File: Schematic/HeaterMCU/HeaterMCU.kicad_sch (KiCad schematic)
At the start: 59 parts, among them J301 To PSU Board, J302 Heater Control, J303 High voltage warning, J304 Firmware, SW301 RESET, U301 Display_IPS_1.3_SPI, U302 ATMEGA328P-AU, U303 TLP185, U304 INA219AIDCNR, U305 TLP185, U306 TPS54302, Y301 8MHz

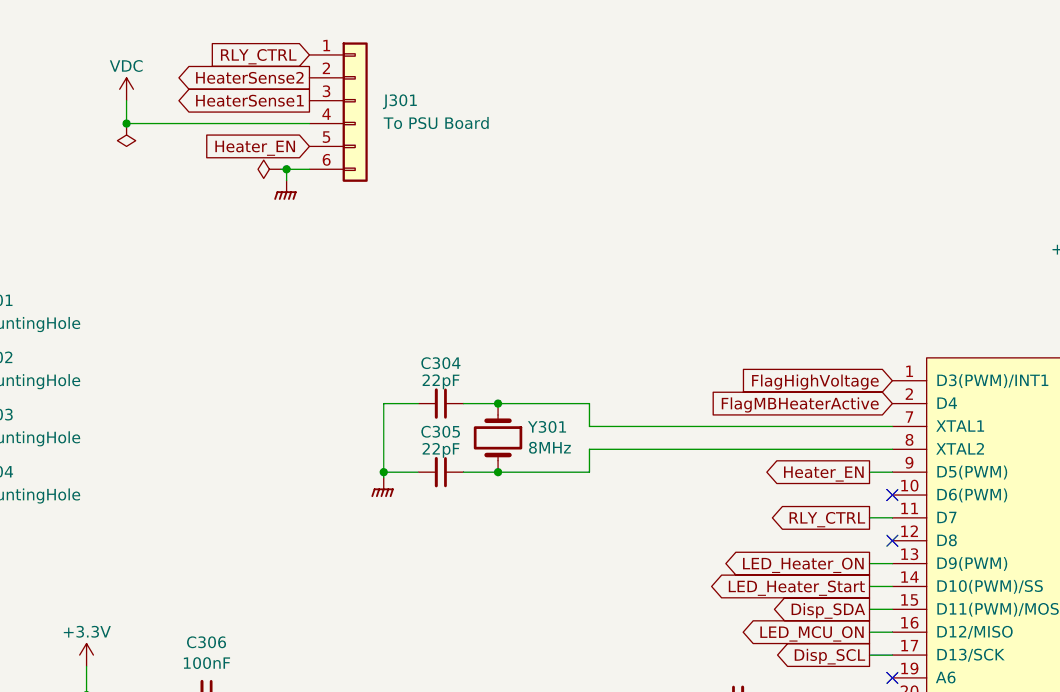
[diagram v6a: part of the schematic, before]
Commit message: Added PWM controlled MOSFET output for soft start
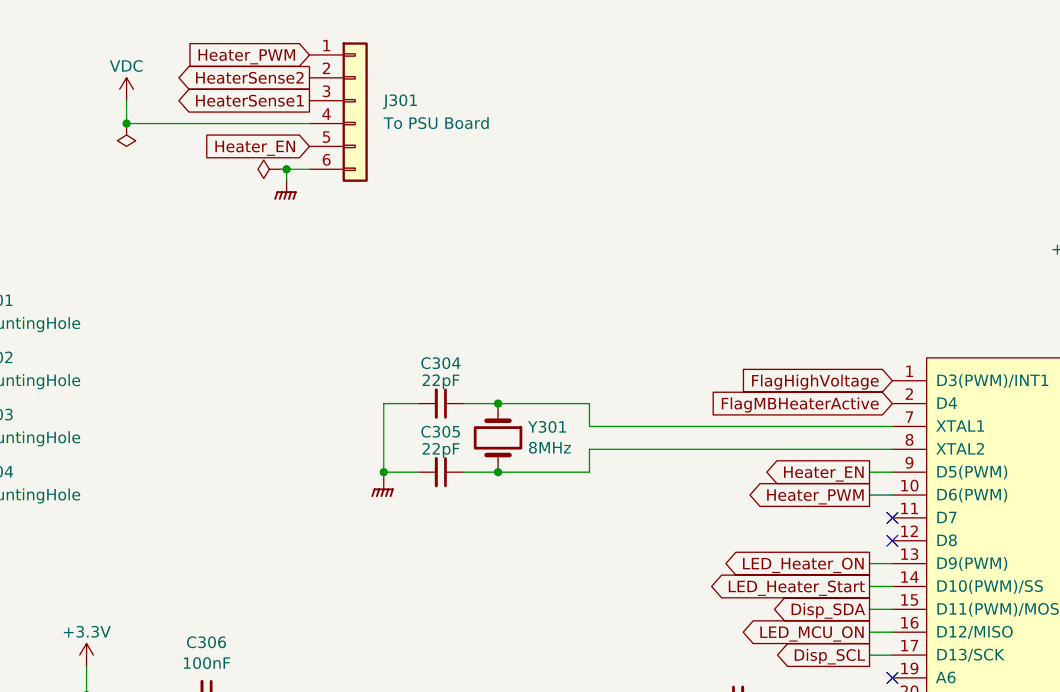
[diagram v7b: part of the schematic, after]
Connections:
- net Heater_PWM: now reaches U302.10 (D6(PWM))
- net Heater_PWM: now also J301.1 (Pin_1)
- net RLY_CTRL: no longer names the net of U302.11 (D7)
- net RLY_CTRL: no longer J301.1 (Pin_1)
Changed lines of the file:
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@@
   (no_connect (at 95.885 133.35))
   (no_connect (at 133.985 90.805))
+  (no_connect (at 133.985 73.025))
   (no_connect (at 133.985 95.885))
-  (no_connect (at 133.985 70.485))
   (no_connect (at 64.77 165.735))
   (no_connect (at 133.985 103.505))
@@
     (stroke (width 0) (type default) (color 0 0 0 0))
   )
-  (wire (pts (xy 131.445 73.025) (xy 133.985 73.025))
+  (wire (pts (xy 131.445 70.485) (xy 133.985 70.485))
     (stroke (width 0) (type default) (color 0 0 0 0))
   )
@@
     )
   )
-  (global_label "RLY_CTRL" (shape output) (at 131.445 73.025 180) (fields_autoplaced)
-    (effects (font (size 1.27 1.27)) (justify right))
-    (property "Intersheet References" "${INTERSHEET_REFS}" (id 0) (at 120.1419 72.9456 0)
+  (global_label "Heater_PWM" (shape output) (at 131.445 70.485 180) (fields_autoplaced)
+    (effects (font (size 1.27 1.27)) (justify right))
+    (property "Intersheet References" "${INTERSHEET_REFS}" (id 0) (at 117.7229 70.4056 0)
       (effects (font (size 1.27 1.27)) (justify right) hide)
     )
@@
     )
   )
-  (global_label "RLY_CTRL" (shape input) (at 69.215 21.59 180) (fields_autoplaced)
-    (effects (font (size 1.27 1.27)) (justify right))
-    (property "Intersheet References" "${INTERSHEET_REFS}" (id 0) (at 57.9119 21.5106 0)
-      (effects (font (size 1.27 1.27)) (justify right) hide)
-    )
+  (global_label "Heater_PWM" (shape input) (at 69.215 21.59 180) (fields_autoplaced)
+    (effects (font (size 1.27 1.27)) (justify right))
+    (property "Intersheet References" "${INTERSHEET_REFS}" (id 0) (at 55.4929 21.5106 0)
+      (effects (font (size 1.27 1.27)) (justify right) hide)
+    )

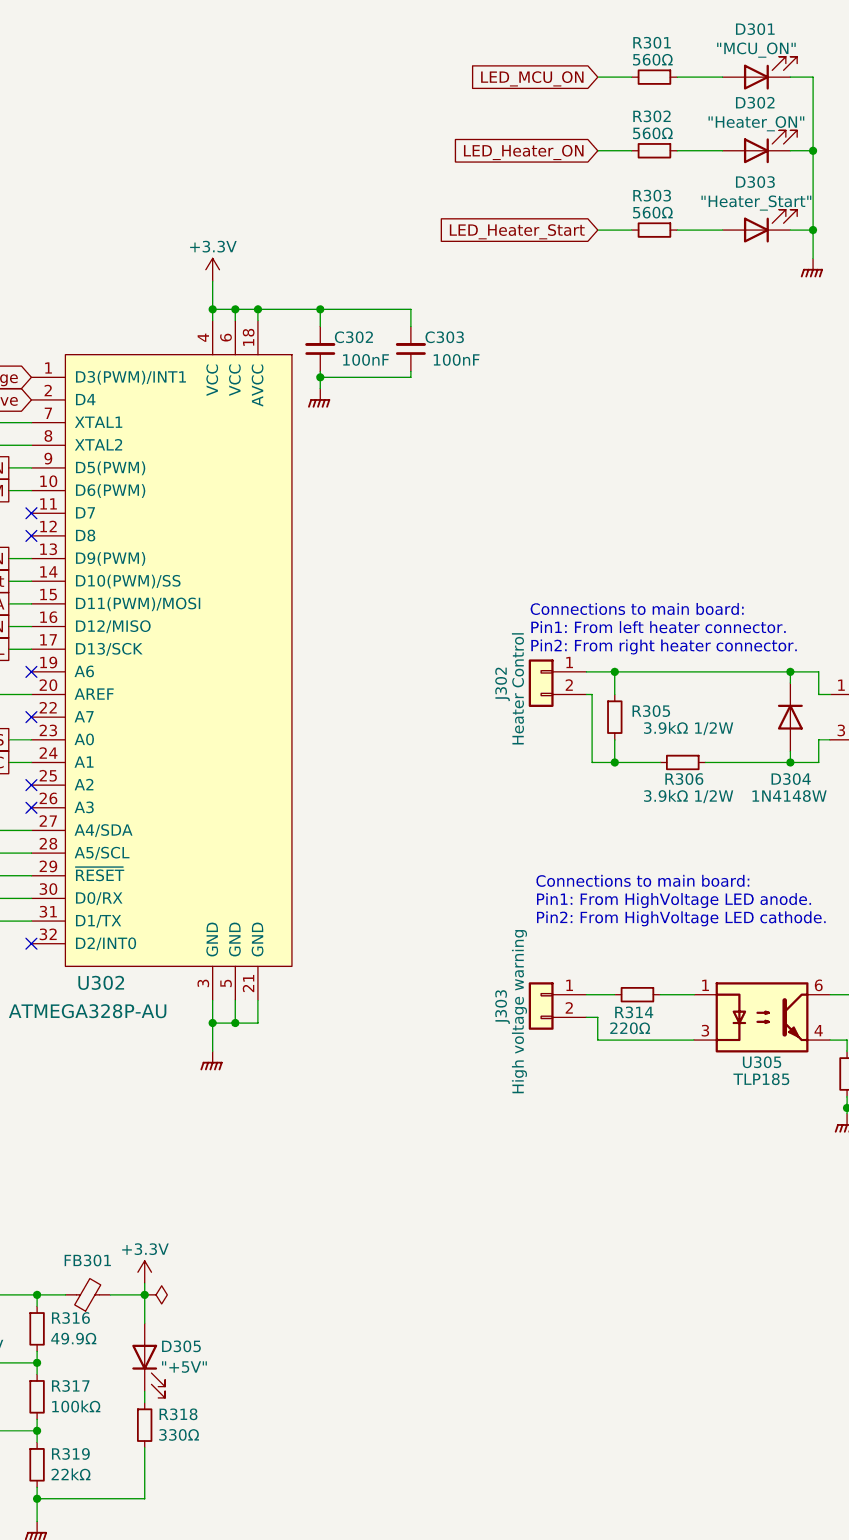
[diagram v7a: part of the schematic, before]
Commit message: Updated component values
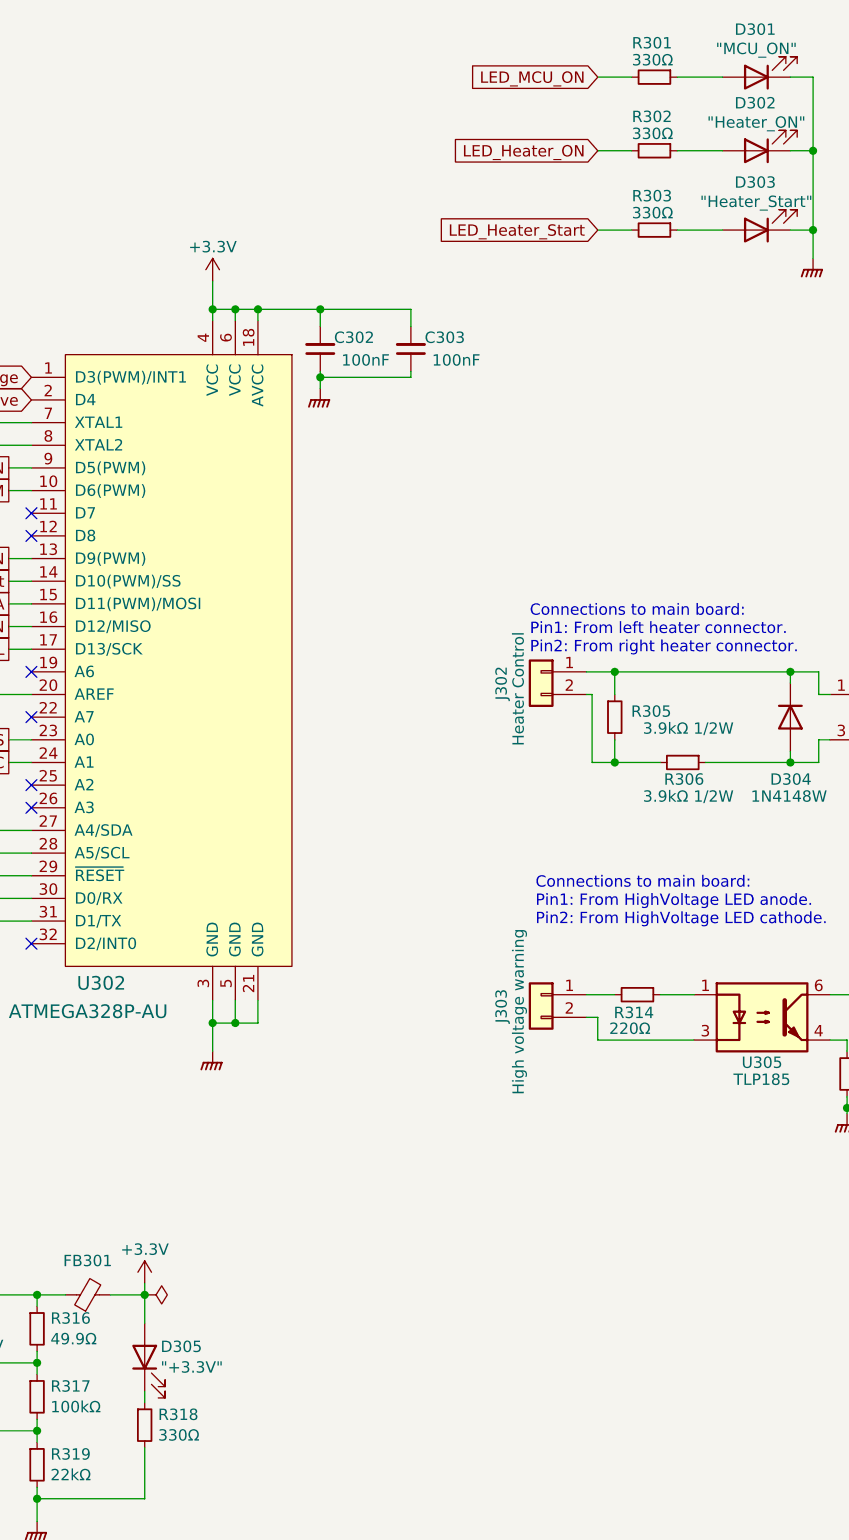
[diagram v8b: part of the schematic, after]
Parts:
- D305: value "+5V" -> "+3.3V"
- R301, R302, R303: value 560Ω -> 330Ω
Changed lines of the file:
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@@
       (effects (font (size 1.27 1.27)) (justify left))
     )
-    (property "Value" "560Ω" (id 1) (at 201.295 30.48 90)
+    (property "Value" "330Ω" (id 1) (at 201.295 30.48 90)
       (effects (font (size 1.27 1.27)) (justify left))
     )
@@
       (effects (font (size 1.27 1.27)) (justify left))
     )
-    (property "Value" "560Ω" (id 1) (at 201.295 39.37 90)
+    (property "Value" "330Ω" (id 1) (at 201.295 39.37 90)
       (effects (font (size 1.27 1.27)) (justify left))
     )
@@
       (effects (font (size 1.27 1.27)) (justify right))
     )
-    (property "Value" "\"+5V\"" (id 1) (at 148.463 168.783 90)
+    (property "Value" "\"+3.3V\"" (id 1) (at 148.463 168.783 90)
       (effects (font (size 1.27 1.27)) (justify right))
     )
@@
       (effects (font (size 1.27 1.27)) (justify left))
     )
-    (property "Value" "560Ω" (id 1) (at 201.295 22.225 90)
+    (property "Value" "330Ω" (id 1) (at 201.295 22.225 90)
       (effects (font (size 1.27 1.27)) (justify left))
     )
@@
     )
     (path "/6f303d0b-208d-42bf-abbe-cd09ce55af24"
-      (reference "D305") (unit 1) (value "\"+5V\"") (footprint "LED_SMD:LED_0603_1608Metric_Pad1.05x0.95mm_HandSolder")
+      (reference "D305") (unit 1) (value "\"+3.3V\"") (footprint "LED_SMD:LED_0603_1608Metric_Pad1.05x0.95mm_HandSolder")
     )
     (path "/328196f7-7481-4b7d-8d89-b35fad318902"
@@
     )
     (path "/70e921c9-9afe-4b38-afa0-ace94eae71a3"
-      (reference "R301") (unit 1) (value "560Ω") (footprint "Resistor_SMD:R_0603_1608Metric_Pad0.98x0.95mm_HandSolder")
+      (reference "R301") (unit 1) (value "330Ω") (footprint "Resistor_SMD:R_0603_1608Metric_Pad0.98x0.95mm_HandSolder")
     )
     (path "/183290ea-f29b-4259-ab3f-5f72f5a8e50e"
-      (reference "R302") (unit 1) (value "560Ω") (footprint "Resistor_SMD:R_0603_1608Metric_Pad0.98x0.95mm_HandSolder")
+      (reference "R302") (unit 1) (value "330Ω") (footprint "Resistor_SMD:R_0603_1608Metric_Pad0.98x0.95mm_HandSolder")
     )
     (path "/202dcc76-70ac-4ba6-8902-b4e09a3a2b08"
-      (reference "R303") (unit 1) (value "560Ω") (footprint "Resistor_SMD:R_0603_1608Metric_Pad0.98x0.95mm_HandSolder")
+      (reference "R303") (unit 1) (value "330Ω") (footprint "Resistor_SMD:R_0603_1608Metric_Pad0.98x0.95mm_HandSolder")
     )
     (path "/76b5ac93-d756-4ab8-b6a3-359b223c85f3"
